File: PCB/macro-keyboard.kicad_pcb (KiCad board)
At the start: 4 copper layers, 77.6 x 43 mm, 39 parts, among them SW1 SW_Push, SW2 SW_Push, SW3 SW_Push, SW4 SW_Push, SW5 SW_Push, SW6 SW_Push, SW7 SW_Push, SW8 SW_Push, U1 PRTR5V0U2X, U2 ATmega32U4-A, Y1 Crystal_GND24_Small

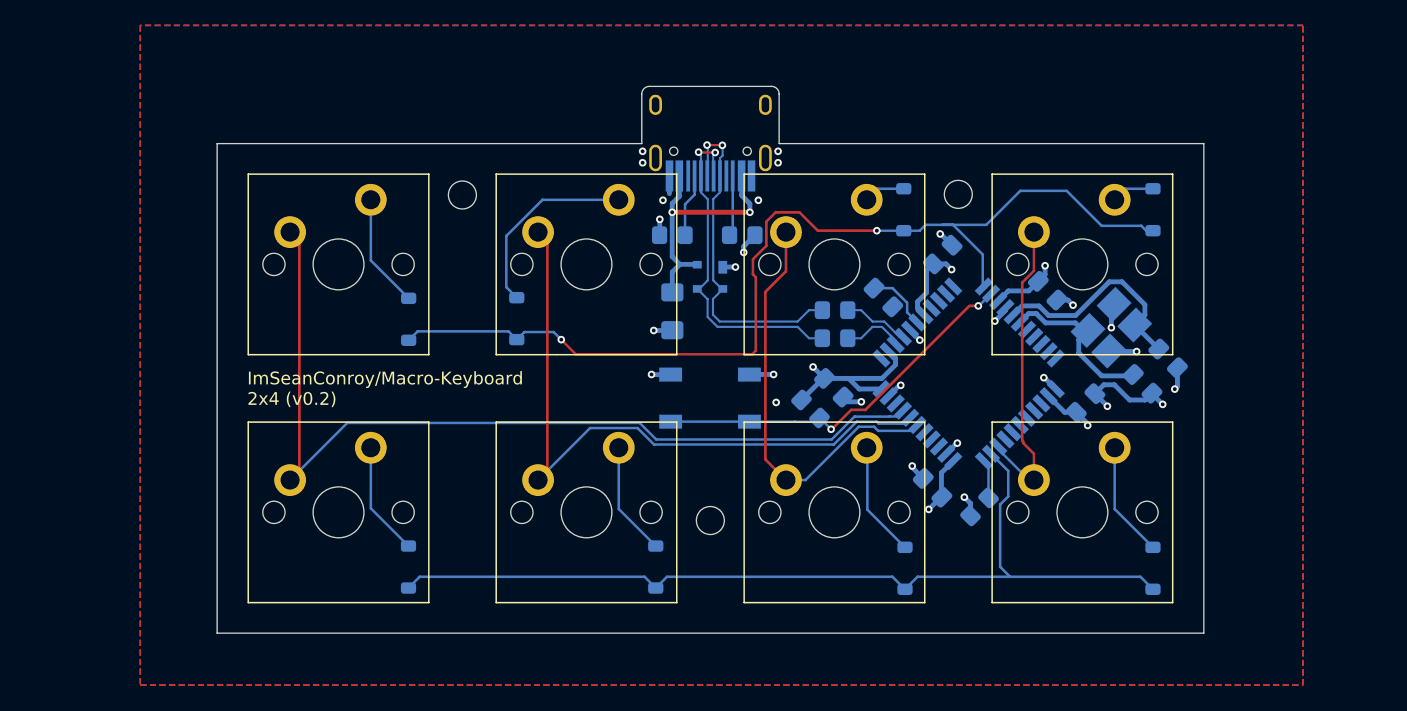
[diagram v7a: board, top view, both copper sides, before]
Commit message: Significantly simplify design
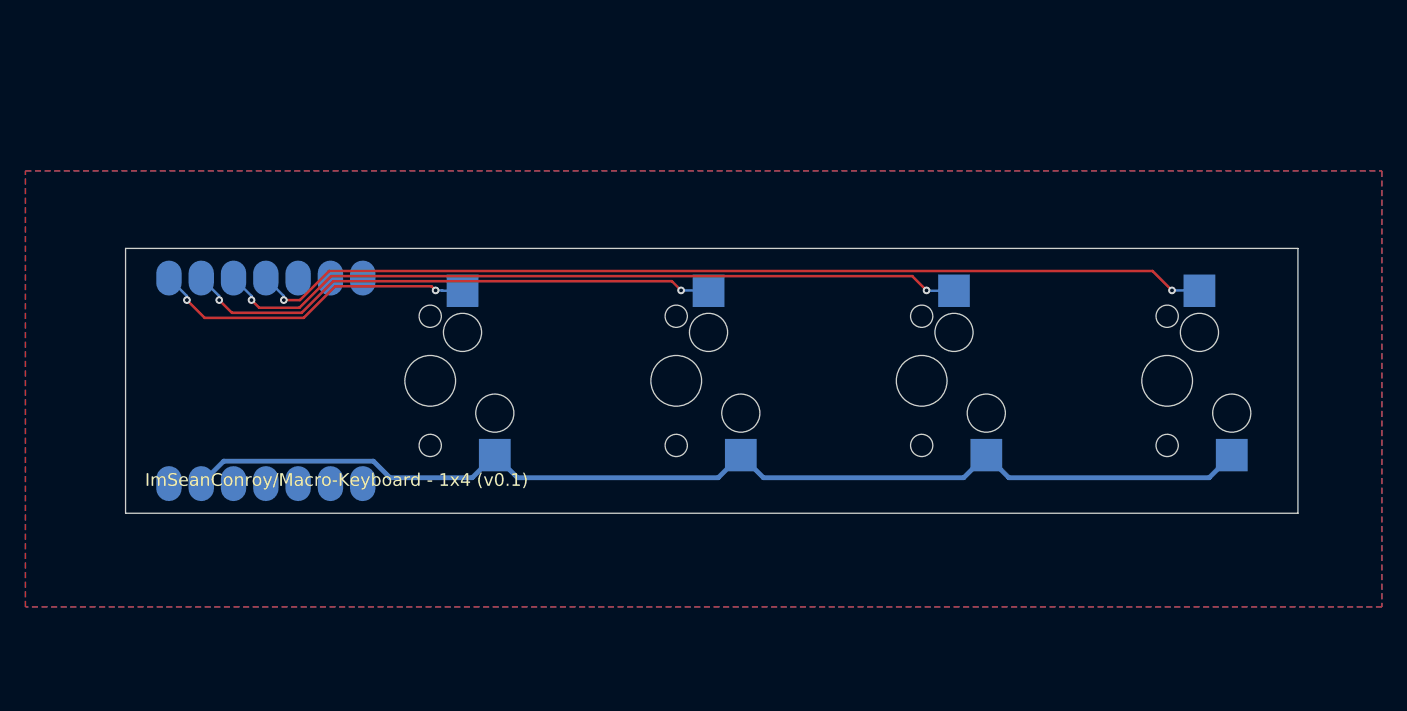
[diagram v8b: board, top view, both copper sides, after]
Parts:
- removed C1, C2: 22p, Capacitor_SMD:C_0805_2012Metric_Pad1.18x1.45mm_HandSolder
- removed C3, C4, C5, C6: 0.1u, Capacitor_SMD:C_0805_2012Metric_Pad1.18x1.45mm_HandSolder
- removed C7: 10u, Capacitor_SMD:C_0805_2012Metric_Pad1.18x1.45mm_HandSolder
- removed C8: 1u, Capacitor_SMD:C_0805_2012Metric_Pad1.18x1.45mm_HandSolder
- removed D1, D2, D3, D4, D5, D6, D7, D8: D, Diode_SMD:D_SOD-123
- removed F1: 500m, Fuse:Fuse_1206_3216Metric_Pad1.42x1.75mm_HandSolder
- removed HOLE1, HOLE2, HOLE3: MountingHole_2.2mm_M2_DIN965, MountingHole:MountingHole_2.2mm_M2_DIN965
- removed R1, R2: 5.1k, Resistor_SMD:R_0805_2012Metric_Pad1.20x1.40mm_HandSolder
- removed R3, R4: 22, Resistor_SMD:R_0805_2012Metric_Pad1.20x1.40mm_HandSolder
- removed R5, R6: 10k, Resistor_SMD:R_0805_2012Metric_Pad1.20x1.40mm_HandSolder
- removed SW13: ~, Button_Switch_SMD:SW_SPST_SKQG_WithStem
- removed SW5, SW6, SW7, SW8: SW_Push, ScottoKeebs_MX:MX_PCB_1.00u
- removed U2: ATmega32U4-A, Package_QFP:TQFP-44_10x10mm_P0.8mm
- removed USB1: HRO-TYPE-C-31-M-12, Type-C:HRO-TYPE-C-31-M-12-HandSoldering
- removed Y1: Crystal_GND24_Small, Crystal:Crystal_SMD_3225-4Pin_3.2x2.5mm_HandSoldering
- SW1, SW2, SW3, SW4: footprint ScottoKeebs_MX:MX_PCB_1.00u -> MX_Only:MXOnly-1U-Hotswap
- U1: value PRTR5V0U2X -> MOUDLE-SEEEDUINO-XIAO-ESP32C3; footprint random-keyboard-parts:SOT143B -> xiao ESP32C3_PCB:MOUDLE14P-SMD-2.54-21X17.8MM
- moved U1 24.4 mm to (77.7, 54.6), turned to -90 degrees
- moved SW1 11.7 mm to (80.1, 63.5), turned to -90 degrees
- moved SW2 11.6 mm to (99.4, 63.5), turned to -90 degrees
- moved SW3 11.4 mm to (118.7, 63.5), turned to -90 degrees
- moved SW4 11.3 mm to (138.0, 63.5), turned to -90 degrees
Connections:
- SW1 pad 1: col0 -> sw1
- SW1 pad 2: Net-(D1-A) -> GND
- SW2 pad 1: col1 -> sw2
- SW2 pad 2: Net-(D2-A) -> GND
- SW3 pad 1: col2 -> sw3
- SW3 pad 2: Net-(D3-A) -> GND
- SW4 pad 1: col3 -> sw4
- SW4 pad 2: Net-(D4-A) -> GND
- U1 pad 1: GND -> sw1
- U1 pad 2: DP -> sw2
- U1 pad 3: DN -> sw3
- U1 pad 4: VCC -> sw4
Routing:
- net +5V: track 113.1 -> 0.00 mm, vias 7 -> 0
- net row0: track 80.2 -> 0.00 mm, vias 2 -> 0
- net sw4: track 0.00 -> 75.9 mm, vias 0 -> 2
- net row1: track 71.7 -> 0.00 mm
- net col0: track 71.6 -> 0.00 mm
- net sw3: track 0.00 -> 59.3 mm, vias 0 -> 2
- net col1: track 52.6 -> 0.00 mm
- net GND: track 40.4 -> 87.5 mm, vias 26 -> 0
- net sw2: track 0.00 -> 42.6 mm, vias 0 -> 2
- net col2: track 33.2 -> 0.00 mm
- net RESET: track 30.1 -> 0.00 mm, vias 2 -> 0
- net DP: track 28.4 -> 0.00 mm, vias 2 -> 0
- net DN: track 28.3 -> 0.00 mm, vias 2 -> 0
- net sw1: track 0.00 -> 25.7 mm, vias 0 -> 2
- net col3: track 24.3 -> 0.00 mm
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- added copper zone on B.Cu, net (none)
- added copper zone on F.Cu, net (none)
- removed copper zone on B.Cu, net GND
- removed copper zone on F.Cu, net GND
- removed copper zone on In1.Cu, net GND
- removed copper zone on In2.Cu, net GND
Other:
- board size 77.6 x 43 mm -> 92.2 x 20.8 mm
- copper layers 4 -> 2
- board text added: "ImSeanConroy/Macro-Keyboard - 1x4 (v0.1)"
- board text removed: "ImSeanConroy/Macro-Keyboard 2x4 (v0.2)"
